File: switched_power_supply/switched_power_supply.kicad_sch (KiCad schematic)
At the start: 38 parts, among them T1 Transformador_1x2, U1 Viper53, U2 TL431, U3 PC817 Opto

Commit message: teste
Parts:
- removed D1, D1c1: 1N4007, DO-41, symbol Sheet1-altium-import:root_2_Diodo 1N4007

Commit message: cu
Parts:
- added D1d2, D1d3: 1N4007, DO-41, symbol Sheet1-altium-import:root_2_Diodo 1N4007
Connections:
- net BarP: now also D1d2.1 (K), D1d3.1 (K)
- net at D1d1.1 (K), L1.3: now also D1d2.2 (A)
- net at D1b1.1 (K), L1.1: now also D1d3.2 (A)

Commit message: a
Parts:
- removed D1b1, D1d1: 1N4007, DO-41, symbol Sheet1-altium-import:root_2_Diodo 1N4007

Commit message: Uploanding files
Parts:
- removed C12b1: Capacitor_Eletrolitico, CE_RAD_8.1_11.2_3.85, symbol Sheet1-altium-import:root_3_Capacitor_Eletrolitico_0
- removed C8: Capacitor_Filme, Capacitor_Ret_11.1_3.64_7.7_9, symbol Sheet1-altium-import:root_3_Capacitor_Filme
- removed U1: Viper53, C__Users_muril_Meu Drive (murilloribeiro2010@gmail.com)_IFSC xDrive_pot2_Footprint.PcbLib:DIP8, symbol Sheet1-altium-import:root_0_Viper53
- added D1d1, D1d4: 1N4007, Diode_THT:D_A-405_P12.70mm_Horizontal, symbol Sheet1-altium-import:root_2_Diodo 1N4007
- added IC1: VIPER53ESPTR-E, pci:SOIC127P1410X370-11N, symbol pci:VIPER53ESPTR-E
- C1: footprint CE_RAD_5.1_11.5_2.75 -> pci:EEHZT1E331UP
- C10: footprint Capacitor_Ret_6.8_2.5_4.9_4.8 -> pci:C1206
- C11: footprint CE_RAD_8.1_11.2_3.85 -> pci:16SVPG330M
- C2: footprint Capacitor 2.2nF -> pci:CAPC1608X97N
- C2b1, C7: footprint CE_RAD_16.2_26_7.7 -> Capacitor_THT:CP_Radial_D16.0mm_P7.50mm
- C3: footprint Capacitor_Ret_ 18_6.6_10.2_14.8 -> Capacitor_THT:C_Rect_L18.0mm_W5.0mm_P15.00mm_FKS3_FKP3
- C3b1: footprint Capacitor_Ret_ 18_6.6_10.2_14.8 -> Capacitor_THT:C_Rect_L18.0mm_W6.0mm_P15.00mm_FKS3_FKP3; VOLTAGE 10nF -> 15nF
- C4: footprint Capacitor 4.7uF -> pci:CAPC3225X94N
- C5: footprint Capacitor_Ret_6.8_2.5_9.2_4.8 -> Capacitor_THT:C_Rect_L7.0mm_W2.5mm_P5.00mm
- C6: footprint Capacitor_Ret_6.8_2.5_9.2_4.8 -> pci:CAPC3216X170N
- C9: footprint CE_RAD_12.7_26.2_4.6 -> pci:EEEFK0J332AV
- D1d2, D1d3: footprint DO-41 -> Diode_THT:D_A-405_P12.70mm_Horizontal
- D2: footprint DO-35 -> Diode_THT:D_DO-35_SOD27_P7.62mm_Horizontal
- D3: footprint DO-41 -> Diode_THT:D_DO-41_SOD81_P7.62mm_Horizontal
- D4: footprint Diodo SR5200 -> Diode_THT:D_DO-201AD_P15.24mm_Horizontal
- F1: footprint Fusivel_3.34_10.5_12.25 -> Fuse:Fuse_Bourns_MF-RG600
- L1: footprint Indutor_Filtro_20.5_14.8_20 -> Inductor_THT:L_Axial_L20.0mm_D8.0mm_P25.40mm_Horizontal
- L2: footprint Indutor 10uH -> pci:INDPM108102X400N
- R1, R2, R3, R5: value Resistor PTH -> Resistor SMD; footprint Resistor 1/8W -> Resistor_SMD:R_0805_2012Metric
- R4: footprint Resistor 5W PTH -> Resistor_THT:R_Axial_Power_L25.0mm_W6.4mm_P30.48mm
- R6, R7, R8: footprint Resistor 1/8W -> Resistor_SMD:R_0805_2012Metric
- T1: footprint TRZ 25.010.2 -> Transformer_SMD:Transformer_Wuerth_750315371
- U2: footprint TO-92 -> pci:SOT95P237X112-3N
- U3: footprint PC817 Opto -> pci:SOIC254P960X420-4N
- V1, V2: footprint KRE X2 -> pci:TerminalBlock_bornier-2_P5.08mm
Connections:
- net Cmp: now also IC1.6 (COMP)
- net Drain: now also IC1.11 (DRAIN)
- net GND: now also D1d1.2 (A), D1d4.2 (A), IC1.10 (SOURCE)
- net Osc: now also IC1.7 (OSC)
- net TOVL: now also IC1.5 (TOVL)
- net Vdd: now also IC1.4 (VDD)
- net at D1d2.2 (A), L1.3: now also D1d4.1 (K)
- net at D1d3.2 (A), L1.1: now also D1d1.1 (K)
- new net: IC1.1 (NC_1), IC1.2 (NC_2), IC1.3 (NC_3)
- new net: IC1.8 (NC_4), IC1.9 (NC_5)
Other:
- moved on the sheet: C1, C2, C4, R1, R2

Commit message: Uploading files
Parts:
- T1: footprint Transformer_SMD:Transformer_Wuerth_750315371 -> pci:TRZ 25.010.2
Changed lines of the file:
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@@
 			)
 		)
-		(property "Footprint" "Transformer_SMD:Transformer_Wuerth_750315371"
+		(property "Footprint" "pci:TRZ 25.010.2"
 			(at 165.354 108.458 0)
 			(effects

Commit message: aula 17.02
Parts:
- removed C2b1: Capacitor_Eletrolitico, Capacitor_THT:CP_Radial_D16.0mm_P7.50mm, symbol Sheet1-altium-import:root_3_Capacitor_Eletrolitico_0
- D4: value SR5200 -> RFN4RSM2S; footprint Diode_THT:D_DO-201AD_P15.24mm_Horizontal -> Package_TO_SOT_SMD:TO-277A
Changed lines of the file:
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@@
-	)
-	(symbol
-		(lib_id "Sheet1-altium-import:root_3_Capacitor_Eletrolitico_0")
-		(at 128.27 46.99 0)
-		(unit 1)
-		(exclude_from_sim no)
-		(in_bom yes)
-		(on_board yes)
-		(dnp no)
-		(property "Reference" "C2b1"
-			(at 131.318 46.736 0)
-			(effects
-				(font
-					(size 1.27 1.27)
-				)
-				(justify left bottom)
-			)
-		)
-		(property "Value" "Capacitor_Eletrolitico"
-			(at 131.318 49.276 0)
-			(effects
-				(font
-					(size 1.27 1.27)
-				)
-				(justify left bottom)
-				(hide yes)
-			)
-		)
-		(property "Footprint" "Capacitor_THT:CP_Radial_D16.0mm_P7.50mm"
-			(at 128.27 46.99 0)
-			(effects
-				(font
-					(size 1.27 1.27)
-				)
-				(hide yes)
-			)
-		)
-		(property "Datasheet" ""
-			(at 128.27 46.99 0)
-			(effects
-				(font
-					(size 1.27 1.27)
-				)
-				(hide yes)
-			)
-		)
-		(property "Description" "Capacitor"
-			(at 128.27 46.99 0)
-			(effects
-				(font
-					(size 1.27 1.27)
-				)
-				(hide yes)
-			)
-		)
-		(property "MANUFACTURER_PART_NUMBER" ""
-			(at 125.222 41.402 0)
-			(effects
-				(font
-					(size 1.27 1.27)
-				)
-				(justify left bottom)
-				(hide yes)
-			)
-		)
-		(property "DATASHEET" ""
-			(at 125.222 41.402 0)
-			(effects
-				(font
-					(size 1.27 1.27)
-				)
-				(justify left bottom)
-				(hide yes)
-			)
-		)
-		(property "ML_PART" ""
-			(at 125.222 41.402 0)
-			(effects
-				(font
-					(size 1.27 1.27)
-				)
-				(justify left bottom)
-				(hide yes)
-			)
-		)
-		(property "SOLDAR" ""
-			(at 125.222 41.402 0)
-			(effects
-				(font
-					(size 1.27 1.27)
-				)
-				(justify left bottom)
-				(hide yes)
-			)
-		)
-		(property "ALTIUM_VALUE" "47uF"
-			(at 130.81 49.53 0)
-			(effects
-				(font
-					(size 1.27 1.27)
-				)
-				(justify left bottom)
-			)
-		)
-		(property "VOLTAGE" ""
-			(at 131.318 51.816 0)
-			(effects
-				(font
-					(size 1.27 1.27)
-				)
-				(justify left bottom)
-				(hide yes)
-			)
-		)
-		(pin "1"
-		)
-		(pin "2"
-		)
-		(instances
-			(project "switched_power_supply"
-				(path "/4773a992-9be3-432c-aff4-e3b29687466a"
-					(reference "C2b1")
-					(unit 1)
-				)
-			)
-		)
 	)
 	(symbol
@@
 			)
 		)
-		(property "Value" "SR5200"
-			(at 185.42 110.236 0)
-			(effects
-				(font
-					(size 1.27 1.27)
-				)
-				(justify left bottom)
-			)
-		)
-		(property "Footprint" "Diode_THT:D_DO-201AD_P15.24mm_Horizontal"
+		(property "Value" "RFN4RSM2S"
+			(at 181.864 109.982 0)
+			(effects
+				(font
+					(size 1.27 1.27)
+				)
+				(justify left bottom)
+			)
+		)
+		(property "Footprint" "Package_TO_SOT_SMD:TO-277A"
 			(at 187.452 105.41 0)
 			(effects
@@
 		)
 		(property "Value" "TL431"
-			(at 189.484 150.876 0)
-			(effects
-				(font
+			(at 182.626 153.416 0)
+			(effects
+				(font

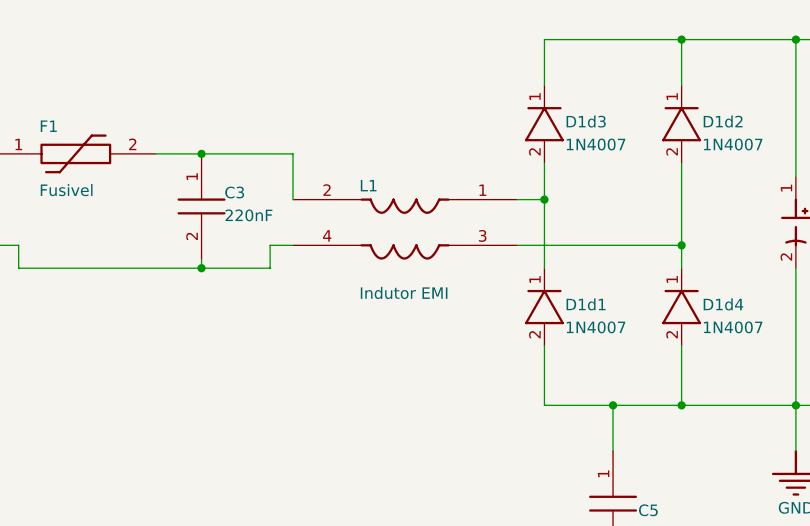
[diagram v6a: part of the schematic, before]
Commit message: footprint EMI ind. corrigido
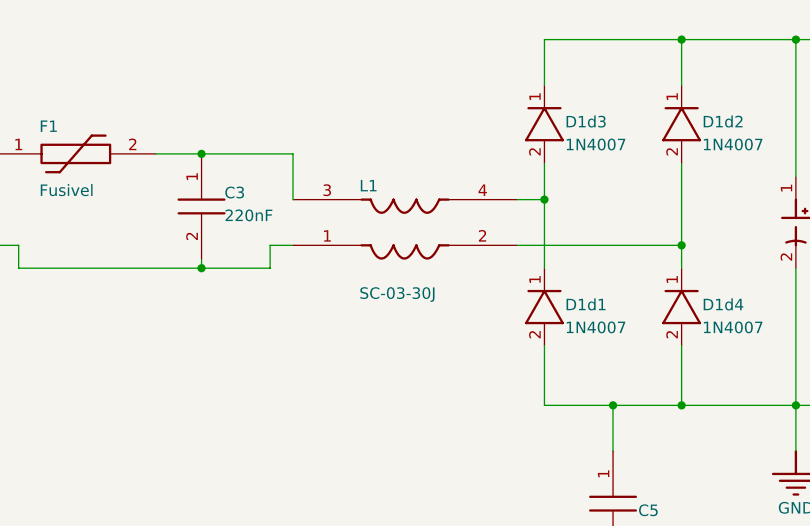
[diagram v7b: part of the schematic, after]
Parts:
- L1: value Indutor EMI -> SC-03-30J
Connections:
- net at D1d2.2 (A), D1d4.1 (K): now also L1.2; no longer L1.3
- net at D1d1.1 (K), D1d3.2 (A): now also L1.4; no longer L1.1
- net at C3.1, F1.2: now also L1.3; no longer L1.2
- net at C3.2, V1.2: now also L1.1; no longer L1.4
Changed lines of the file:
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@@
 			)
 		)
-		(property "Value" "Indutor EMI"
+		(property "Value" "SC-03-30J"
 			(at 69.596 55.626 0)
 			(effects

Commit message: pcb atualizado
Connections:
- net at T1.2: now also D4.3 (A); no longer D4.2 (A)
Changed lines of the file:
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@@
 		(pin "1"
 		)
-		(pin "2"
+		(pin "3"
 		)
 		(instances
